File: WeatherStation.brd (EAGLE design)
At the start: 30.5 x 53.3 mm, 36 parts, among them J1 EDISON_CONNECTOR_FULLMOUNTING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, J2 EDISON_CONNECTOR_FULLHEADER, U1 MCP73831, U2 HTU21D, U3 MPL3115A2, U4 PCA9306

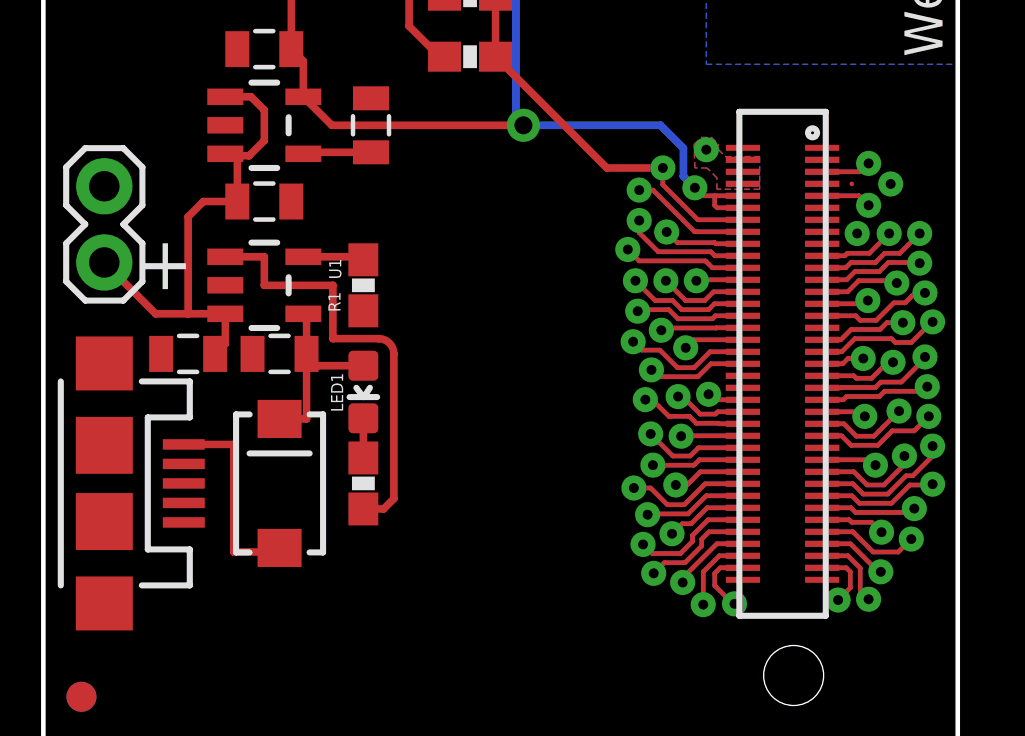
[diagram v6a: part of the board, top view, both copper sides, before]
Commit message: angled some right angled traces
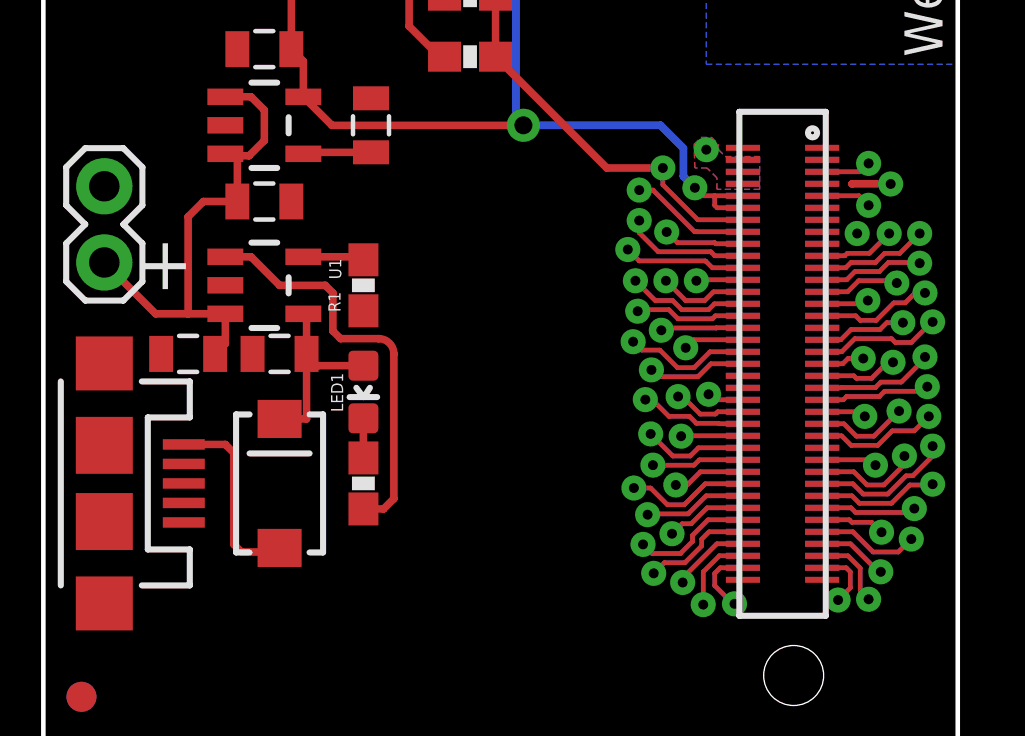
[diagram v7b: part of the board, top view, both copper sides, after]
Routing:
- net GND: track 46.4 -> 47.7 mm
- net N$5: track 14.5 -> 13.7 mm
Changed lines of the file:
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@@
 <wire x1="7.874" y1="45.72" x2="7.874" y2="42.672" width="0.254" layer="1"/>
 <wire x1="8.612" y1="49.276" x2="9.398" y2="49.276" width="0.254" layer="1"/>
+<wire x1="28.2392" y1="22.1798" x2="28.2448" y2="22.1742" width="0.254" layer="1"/>
+<wire x1="28.2392" y1="22.1798" x2="26.955" y2="22.1798" width="0.254" layer="1"/>
+<wire x1="26.955" y1="22.1798" x2="26.9494" y2="22.1742" width="0.254" layer="1"/>
 <wire x1="25.96" y1="22.9798" x2="25.96" y2="22.98" width="0" layer="19" extent="1-16"/>
 <wire x1="25.96" y1="22.18" x2="25.96" y2="22.98" width="0" layer="19" extent="16-16"/>
@@
 <wire x1="25.96" y1="20.18" x2="25.96" y2="20.58" width="0" layer="19" extent="16-16"/>
 <wire x1="25.96" y1="20.1798" x2="25.96" y2="20.18" width="0" layer="19" extent="1-16"/>
-<wire x1="26.9438" y1="22.1798" x2="25.96" y2="22.18" width="0" layer="19" extent="1-16"/>
+<wire x1="26.955" y1="22.1798" x2="25.96" y2="22.18" width="0" layer="19" extent="1-16"/>
 <wire x1="27.1272" y1="20.5232" x2="25.96" y2="20.58" width="0" layer="19" extent="16-16"/>
-<wire x1="28.2448" y1="22.1742" x2="26.9438" y2="22.1798" width="0" layer="19" extent="1-1"/>
 <wire x1="11.938" y1="36.322" x2="13.716" y2="34.682" width="0" layer="19" extent="1-1"/>
 <wire x1="10.914" y1="35.152" x2="11.938" y2="36.322" width="0" layer="19" extent="1-1"/>
@@
 <contactref element="JP1" pad="VBUS"/>
 <contactref element="D1" pad="A"/>
-<wire x1="4.682" y1="13.492" x2="6.35" y2="13.492" width="0.254" layer="1"/>
-<wire x1="6.35" y1="13.492" x2="6.35" y2="9.906" width="0.254" layer="1"/>
-<wire x1="6.35" y1="9.906" x2="7.874" y2="9.906" width="0.254" layer="1"/>
-<wire x1="7.874" y1="9.906" x2="7.874" y2="10.042" width="0.254" layer="1"/>
+<wire x1="4.682" y1="13.492" x2="6.066" y2="13.492" width="0.254" layer="1"/>
+<wire x1="6.066" y1="13.492" x2="6.35" y2="13.208" width="0.254" layer="1"/>
+<wire x1="6.35" y1="13.208" x2="6.35" y2="10.16" width="0.254" layer="1"/>
+<wire x1="6.35" y1="10.16" x2="6.604" y2="9.906" width="0.254" layer="1"/>
+<wire x1="6.604" y1="9.906" x2="7.738" y2="9.906" width="0.254" layer="1"/>
+<wire x1="7.738" y1="9.906" x2="7.874" y2="10.042" width="0.254" layer="1"/>
 </signal>
 <signal name="N$2">
@@
 <contactref element="R2" pad="1"/>
 <contactref element="U1" pad="1"/>
-<wire x1="6.0659" y1="19.746" x2="7.366" y2="19.746" width="0.254" layer="1"/>
-<wire x1="7.366" y1="19.746" x2="7.366" y2="18.796" width="0.254" layer="1"/>
-<wire x1="7.366" y1="18.796" x2="9.652" y2="18.796" width="0.254" layer="1"/>
-<wire x1="9.652" y1="18.796" x2="9.652" y2="17.018" width="0.254" layer="1"/>
-<wire x1="9.652" y1="17.018" x2="11.176" y2="17.018" width="0.254" layer="1"/>
 <wire x1="11.176" y1="17.018" x2="11.684" y2="16.51" width="0.254" layer="1" curve="-90"/>
 <wire x1="11.684" y1="16.51" x2="11.684" y2="11.684" width="0.254" layer="1"/>
 <wire x1="11.684" y1="11.684" x2="11.342" y2="11.342" width="0.254" layer="1"/>
 <wire x1="11.342" y1="11.342" x2="10.668" y2="11.342" width="0.254" layer="1"/>
+<wire x1="6.0659" y1="19.746" x2="6.924" y2="19.746" width="0.254" layer="1"/>
+<wire x1="6.924" y1="19.746" x2="7.874" y2="18.796" width="0.254" layer="1"/>
+<wire x1="7.874" y1="18.796" x2="9.398" y2="18.796" width="0.254" layer="1"/>
+<wire x1="9.398" y1="18.796" x2="9.652" y2="18.542" width="0.254" layer="1"/>
+<wire x1="9.652" y1="18.542" x2="9.652" y2="17.272" width="0.254" layer="1"/>
+<wire x1="9.652" y1="17.272" x2="9.906" y2="17.018" width="0.254" layer="1"/>
+<wire x1="9.906" y1="17.018" x2="11.176" y2="17.018" width="0.254" layer="1"/>
 </signal>
 <signal name="VBAT">
